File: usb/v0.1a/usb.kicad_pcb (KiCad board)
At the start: 2 copper layers, 41 x 20.3 mm, 2 parts, among them J1 PMOD

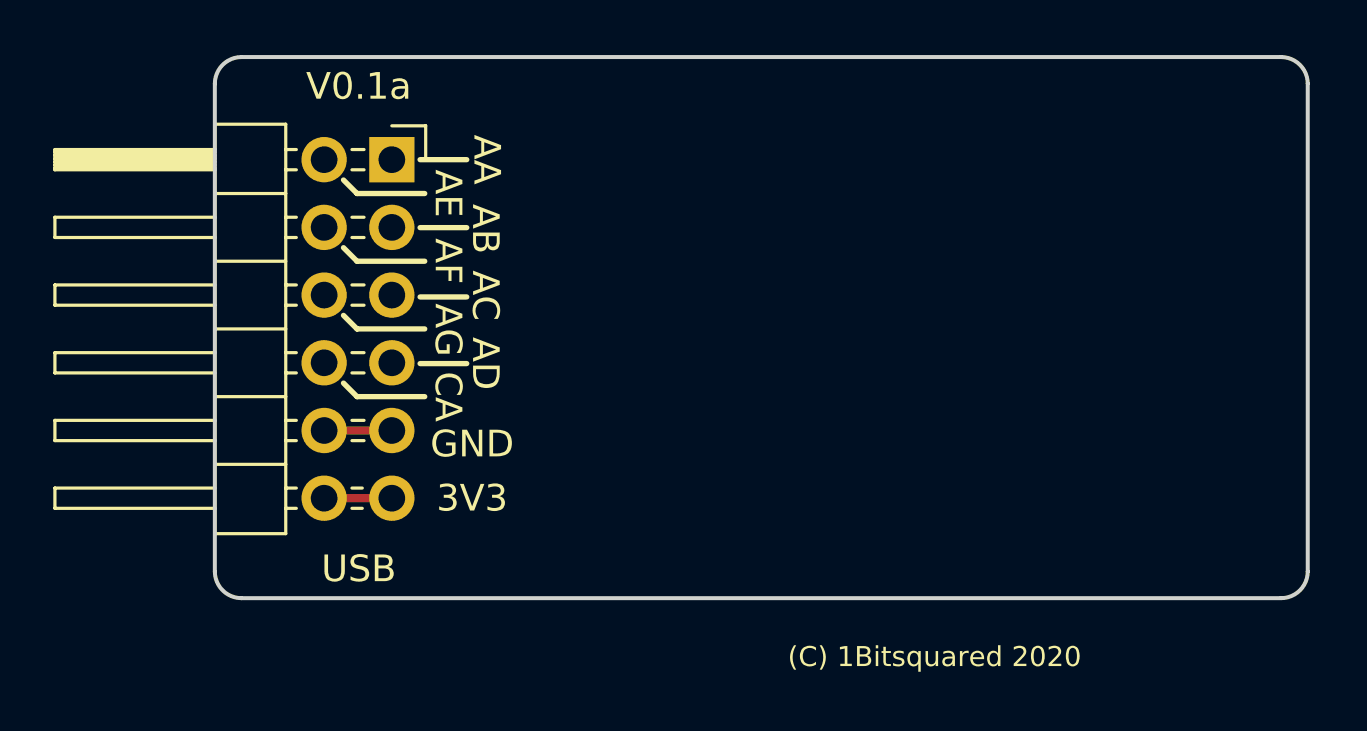
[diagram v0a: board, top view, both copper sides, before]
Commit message: USB Pmod: Finished layout.
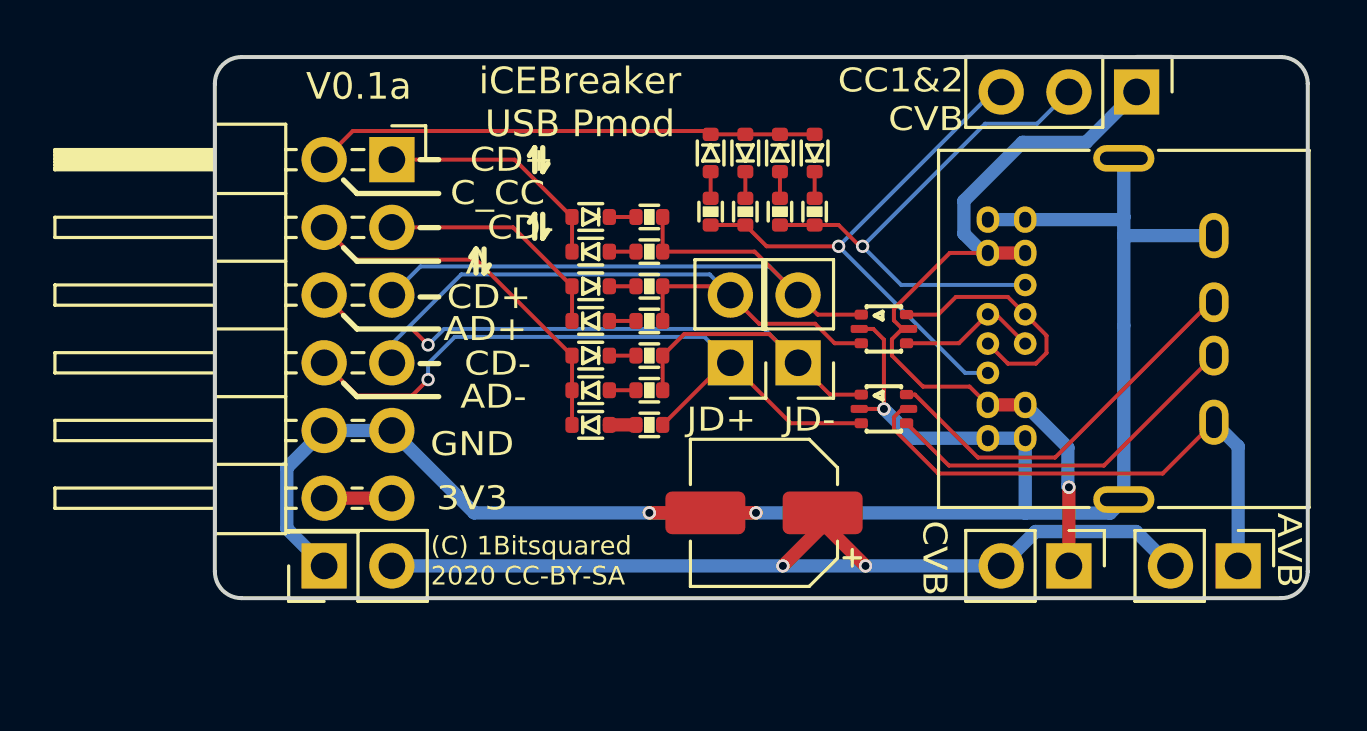
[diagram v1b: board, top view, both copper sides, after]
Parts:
- removed the REF** at (52.7, 40.2)
- added C1: 150u, Capacitor_SMD:CP_Elec_5x3.9, F.Cu at (50.6, 47.1)
- added D1: ~~800mVf, pkl_dipol:D_SOD-523, F.Cu at (44.1, 41.2)
- added D10: ~~800mVf, pkl_dipol:D_SOD-523, F.Cu at (52.5, 33.6)
- added D11: ~~800mVf, pkl_dipol:D_SOD-523, F.Cu at (51.2, 33.6)
- added D2: ~~800mVf, pkl_dipol:D_SOD-523, F.Cu at (44.1, 42.5)
- added D3: ~~800mVf, pkl_dipol:D_SOD-523, F.Cu at (44.1, 43.8)
- added D4: ~~800mVf, pkl_dipol:D_SOD-523, F.Cu at (44.1, 36.0)
- added D5: ~~800mVf, pkl_dipol:D_SOD-523, F.Cu at (44.1, 37.3)
- added D6: ~~800mVf, pkl_dipol:D_SOD-523, F.Cu at (44.1, 38.6)
- added D7: ~~800mVf, pkl_dipol:D_SOD-523, F.Cu at (44.1, 39.9)
- added D8: ~~800mVf, pkl_dipol:D_SOD-523, F.Cu at (49.9, 33.6)
- added D9: ~~800mVf, pkl_dipol:D_SOD-523, F.Cu at (48.6, 33.6)
- added J2: USB_AC_Combo_Receptacle_USB2.0, pkl_connectors:USB_A_C_Receptacle_AdamTech_USB-C31-A-D-VT-CS1, F.Cu at (64.1, 40.2)
- added J3: USBC_CC, Connector_PinHeader_2.54mm:PinHeader_1x03_P2.54mm_Vertical, F.Cu at (64.6, 31.3)
- added J4: JVBUSA, Connector_PinHeader_2.54mm:PinHeader_1x02_P2.54mm_Vertical, F.Cu at (68.4, 49.1)
- added J5: JDP, Connector_PinHeader_2.54mm:PinHeader_1x02_P2.54mm_Vertical, F.Cu at (51.9, 41.5)
- added J6: JDM, Connector_PinHeader_2.54mm:PinHeader_1x02_P2.54mm_Vertical, F.Cu at (49.3, 41.5)
- added J7: AUX5V, Connector_PinSocket_2.54mm:PinSocket_2x01_P2.54mm_Vertical, F.Cu at (34.1, 49.1)
- added J8: JVBUSC, Connector_PinHeader_2.54mm:PinHeader_1x02_P2.54mm_Vertical, F.Cu at (62.0, 49.1)
- added R1: 1.1K, pkl_dipol:R_0402, F.Cu at (46.3, 41.2)
- added R10: 1.1K, pkl_dipol:R_0402, F.Cu at (46.3, 38.6)
- added R11: 12K, pkl_dipol:R_0402, F.Cu at (46.3, 39.9)
- added R2: 12K, pkl_dipol:R_0402, F.Cu at (46.3, 43.8)
- added R3: 12K, pkl_dipol:R_0402, F.Cu at (46.3, 42.5)
- added R4: 1.1K, pkl_dipol:R_0402, F.Cu at (46.3, 36.0)
- added R5: 36K, pkl_dipol:R_0402, F.Cu at (49.9, 35.8)
- added R6: 5.1K, pkl_dipol:R_0402, F.Cu at (48.6, 35.8)
- added R7: 36K, pkl_dipol:R_0402, F.Cu at (52.5, 35.8)
- added R8: 5.1K, pkl_dipol:R_0402, F.Cu at (51.2, 35.8)
- added R9: 12K, pkl_dipol:R_0402, F.Cu at (46.3, 37.3)
- added REF**: null_Logo_SilkS_5mm, pkl_logos:null_Logo_SilkS_5mm, B.Cu at (52.1, 33.6)
- added U1: USBLC6-2, pkl_housings_sot:SOT-666, F.Cu at (55.1, 43.2)
- added U2: USBLC6-2, pkl_housings_sot:SOT-666, F.Cu at (55.1, 40.2)
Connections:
- J1 pad 1: /AA -> /USBC_DP_PUPD
- J1 pad 10: /CAT -> /USBA_DM
- J1 pad 12: +3V3 -> (no net)
- J1 pad 2: /AB -> /USBC_DM_PUPD
- J1 pad 3: /AC -> /USBC_DP
- J1 pad 4: /AD -> /USBC_DM
- J1 pad 6: +3V3 -> (no net)
- J1 pad 7: /AE -> /USBC_CC
- J1 pad 8: /AF -> /USBA_PUPD
- J1 pad 9: /AG -> /USBA_DP
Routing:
- net GND: track 2.54 -> 76.2 mm, vias 0 -> 3
- net +5V: track 0.00 -> 35.5 mm, vias 0 -> 2
- net /USBC_VBUS: track 0.00 -> 31.4 mm, vias 0 -> 1
- net /USBA_DP: track 0.00 -> 29.4 mm, vias 0 -> 1
- net /USBA_DM: track 0.00 -> 26.8 mm, vias 0 -> 1
- net /USBC_DP: track 0.00 -> 25.9 mm
- net /USBC_DM: track 0.00 -> 24.4 mm
- net /CC1: track 0.00 -> 21.2 mm, vias 0 -> 1
- net /USBA_VBUS: track 0.00 -> 20.4 mm
- net /CC2: track 0.00 -> 20.3 mm, vias 0 -> 1
- net /USBC_CC: track 0.00 -> 18.9 mm
- net /xUSBA_DP: track 0.00 -> 14.9 mm
- net /xUSBA_DM: track 0.00 -> 13.9 mm
- net /USBA_PUPD: track 0.00 -> 13.9 mm
- net /xUSBC_DP: track 0.00 -> 9.45 mm
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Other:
- board text added: "(C) 1Bitsquared 2020 CC-BY-SA"
- board text added: "+5V"
- board text added: "A"
- board text added: "AD+"
- board text added: "AD-"
- board text added: "AVB"
- board text added: "CC1&2 CVB"
- board text added: "CD+"
- board text added: "CD-"
- board text added: "CVB"
- board text added: "C_CC"
- board text added: "JD+"
- board text added: "JD-"
- board text added: "iCEBreaker USB Pmod"
- board text removed: "AA"
- board text removed: "AB"
- board text removed: "AC"
- board text removed: "AD"
- board text removed: "AE"
- board text removed: "AF"
- board text removed: "AG"
- board text removed: "CA"
- board text removed: "USB"
- board text removed: "iCEBreaker PMOD USB"

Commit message: USB Pmod: Routing iprovements minor Silkscreen polish.
* The ESD diodes are now optional. They are internally connected
anyways, so we connected them externally too, so that when they are not
populated the data lines are connected.
* Added a note that the large capacitor for host mode is just optional
and might cause issues when used.
* Added the ⇅ symbol to C_CC and expanded A to be AD for clarity on the silkscreen.
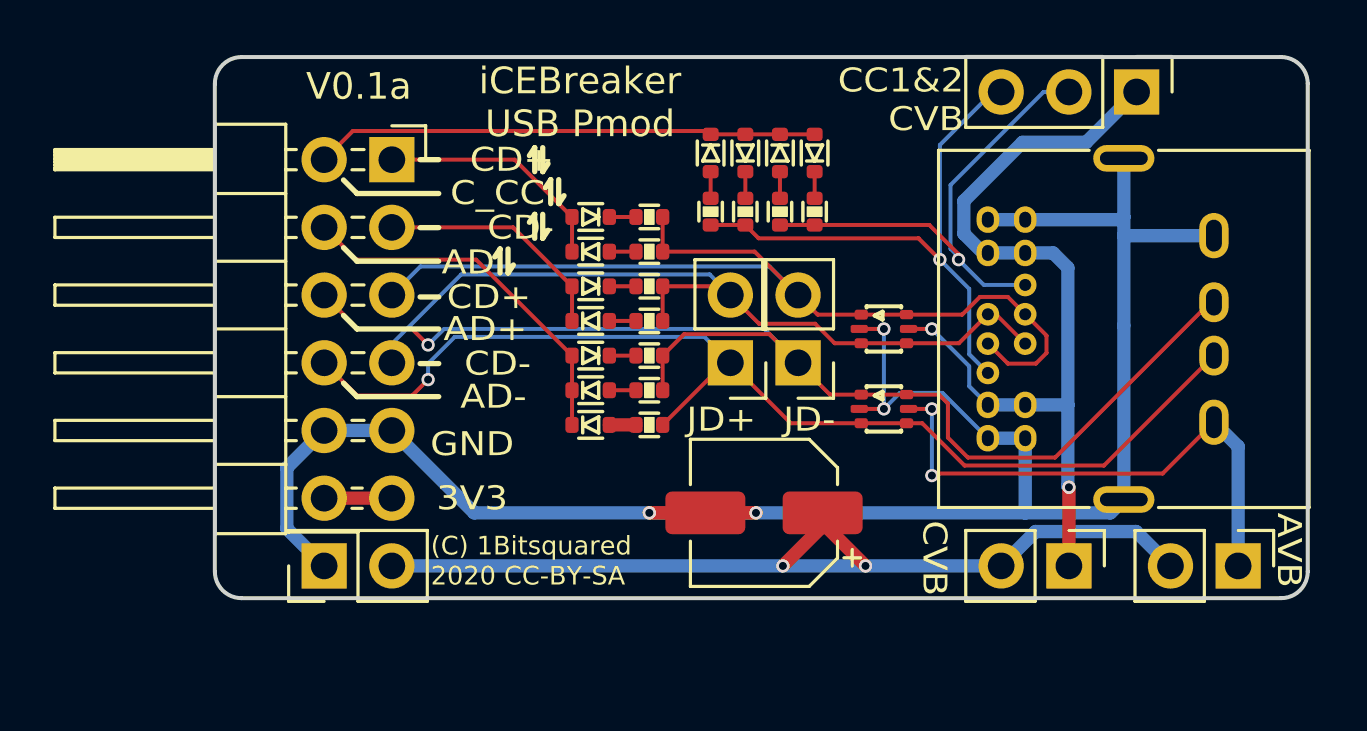
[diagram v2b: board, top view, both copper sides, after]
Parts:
- C1: value 150u -> DNP
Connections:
- J2 pad 2: /xUSBA_DM -> /USBA_DM
- J2 pad 3: /xUSBA_DP -> /USBA_DP
- J2 pad A6: /xUSBC_DP -> /USBC_DP
- J2 pad A7: /xUSBC_DM -> /USBC_DM
- J2 pad B6: /xUSBC_DP -> /USBC_DP
- J2 pad B7: /xUSBC_DM -> /USBC_DM
- U1 pad 4: /xUSBA_DM -> /USBA_DM
- U1 pad 6: /xUSBA_DP -> /USBA_DP
- U2 pad 4: /xUSBC_DM -> /USBC_DM
- U2 pad 6: /xUSBC_DP -> /USBC_DP
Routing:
- net /USBA_DP: track 29.4 -> 46.7 mm
- net /USBA_DM: track 26.8 -> 42.4 mm
- net /xUSBA_DP: track 14.9 -> 0.00 mm
- net /xUSBA_DM: track 13.9 -> 0.00 mm
- net /USBC_DP: track 25.9 -> 37.0 mm
- net /xUSBC_DP: track 9.45 -> 0.00 mm
- net /USBC_DM: track 24.4 -> 31.5 mm
- net /xUSBC_DM: track 5.36 -> 0.00 mm
- net /USBC_VBUS: track 31.4 -> 32.6 mm, vias 1 -> 2
- net /CC2: track 20.3 -> 19.1 mm
- net GND: track 76.2 -> 77.0 mm, vias 3 -> 4
- net /USBA_VBUS: track 20.4 -> 20.6 mm, vias 0 -> 2
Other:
- board text added: "AD"
- board text removed: "A"

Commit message: USB Pmod: Added some F.Cu power jumpers.
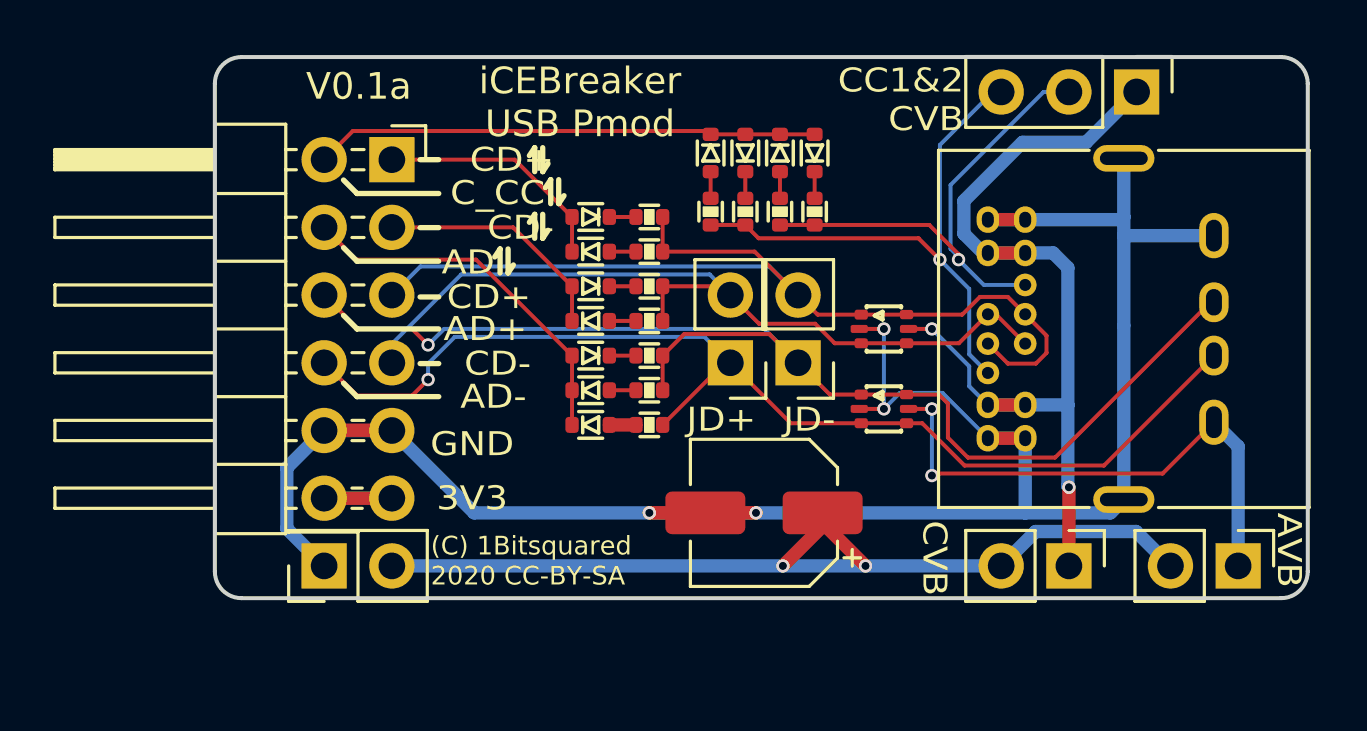
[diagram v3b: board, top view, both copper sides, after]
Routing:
- net GND: track 77.0 -> 82.3 mm
- net /USBC_VBUS: track 32.6 -> 35.4 mm
- net (no net): track 2.54 -> 5.08 mm
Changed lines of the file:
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@@
     (thickness 1.6)
     (drawings 105)
-    (tracks 205)
+    (tracks 211)
     (zones 0)
     (modules 34)
@@
   (gr_line (start 31 30) (end 70 30) (layer Edge.Cuts) (width 0.15))
   (segment (start 34.1 46.55) (end 36.64 46.55) (width 0.5) (layer F.Cu) (net 0))
+  (segment (start 34.1 46.55) (end 36.64 46.55) (width 0.5) (layer B.Cu) (net 0))
   (segment (start 59 36.1) (end 60.4 36.1) (width 0.5) (layer B.Cu) (net 1))
   (segment (start 36.64 44.01) (end 34.1 44.01) (width 0.5) (layer B.Cu) (net 1))
@@
   (segment (start 55.1 43.2) (end 55.1 40.2) (width 0.15) (layer B.Cu) (net 1))
   (segment (start 55.1 40.2) (end 54.175 40.2) (width 0.15) (layer F.Cu) (net 1))
+  (segment (start 36.64 44) (end 34.1 44) (width 0.5) (layer F.Cu) (net 1))
+  (segment (start 59 36.1) (end 60.4 36.1) (width 0.5) (layer F.Cu) (net 1))
+  (segment (start 59 44.3) (end 60.4 44.3) (width 0.5) (layer F.Cu) (net 1))
   (segment (start 44.8 41.2) (end 45.8 41.2) (width 0.15) (layer F.Cu) (net 2))
   (segment (start 43.4 43.8) (end 43.4 42.5) (width 0.15) (layer F.Cu) (net 3))
@@
   (segment (start 58.3 41.6) (end 58.3 42.35) (width 0.15) (layer B.Cu) (net 23))
   (segment (start 56.9 40.2) (end 58.3 41.6) (width 0.15) (layer B.Cu) (net 23))
+  (segment (start 60.4 43.05) (end 59 43.05) (width 0.5) (layer F.Cu) (net 23))
+  (segment (start 59 37.35) (end 60.4 37.35) (width 0.5) (layer F.Cu) (net 23))
   (segment (start 57.136734 45.62503) (end 65.55497 45.62503) (width 0.15) (layer F.Cu) (net 24) (status 40000))
   (segment (start 65.55497 45.62503) (end 67.48 43.7) (width 0.15) (layer F.Cu) (net 24))
